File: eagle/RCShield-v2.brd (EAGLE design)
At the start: 92.7 x 82.5 mm, 52 parts, among them J1/J2 JOYSTICKPTH, P1/P3 POT, P2/P4 POT, Q1 MMBT3906, U1 TOUSCRUINO_SHIELD, U2 FT232RL-BASICSSOP, U4 XBEE, X1 USBSMD

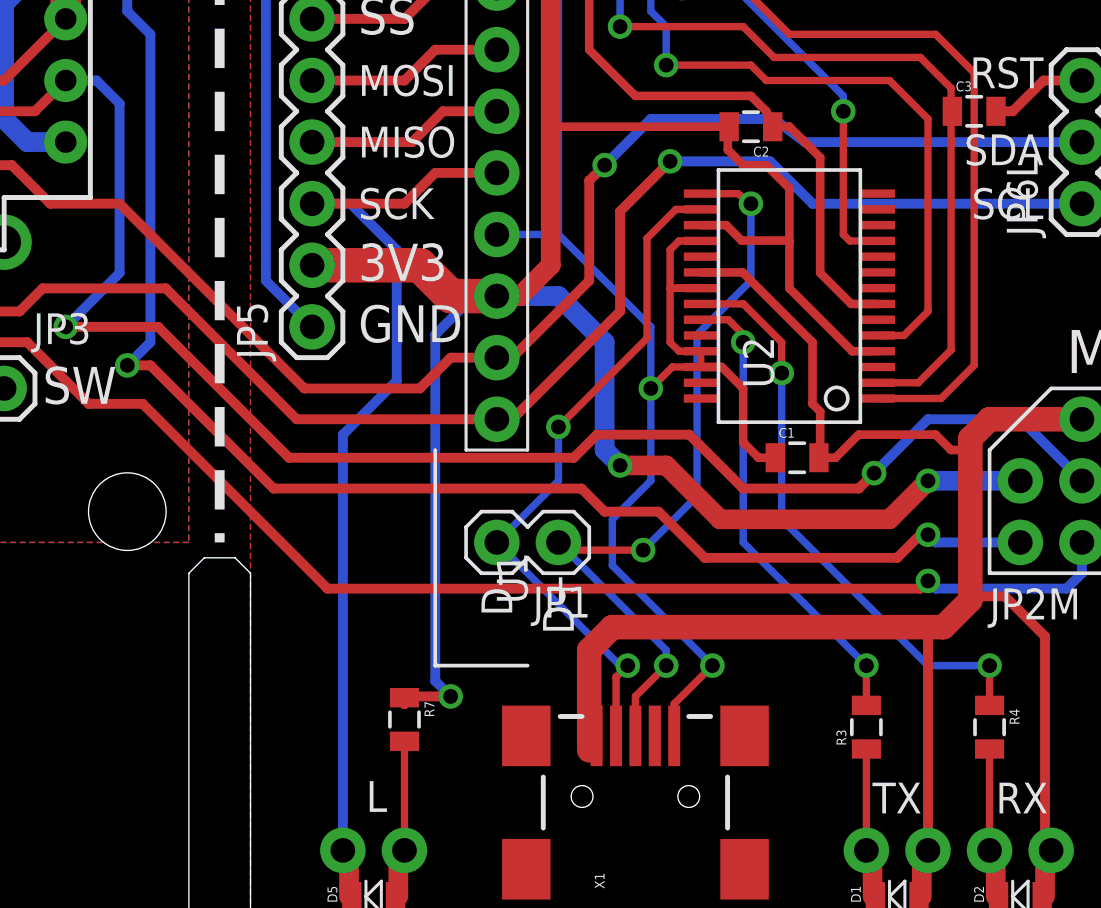
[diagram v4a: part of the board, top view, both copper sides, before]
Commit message: 
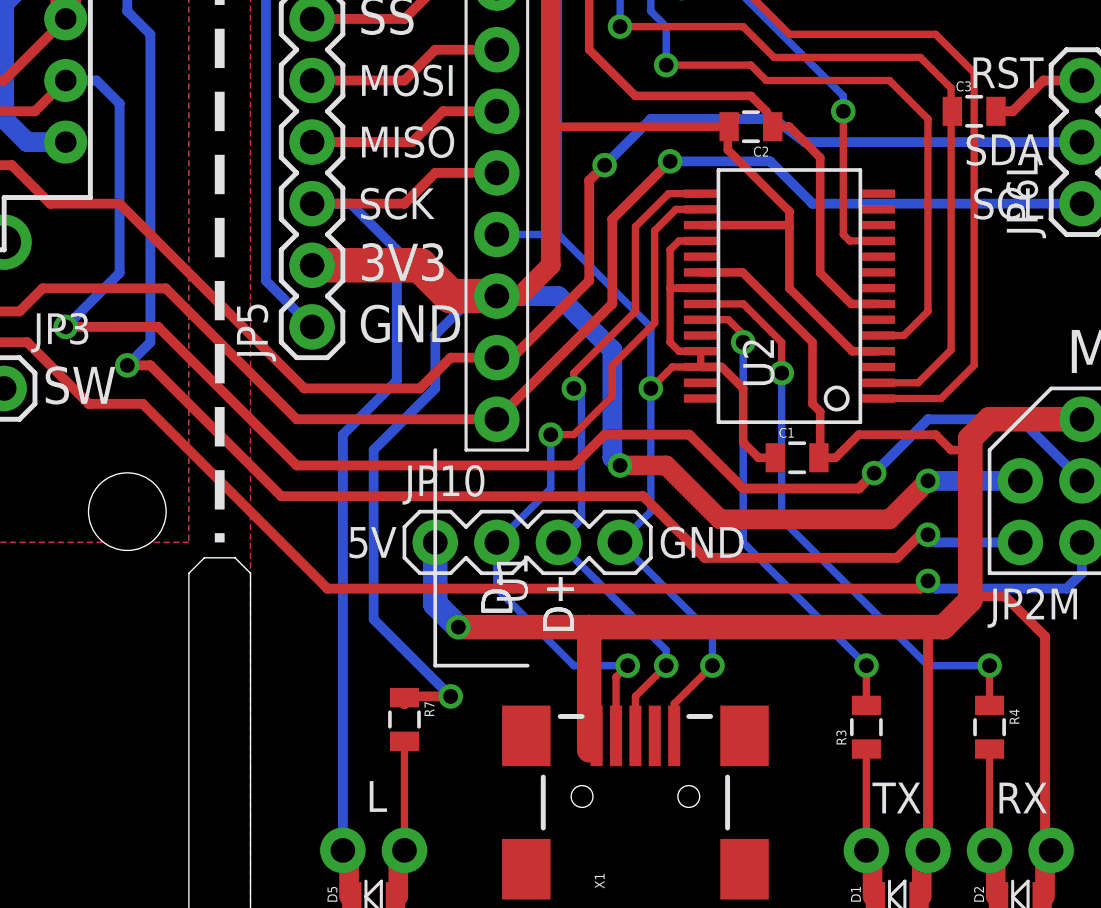
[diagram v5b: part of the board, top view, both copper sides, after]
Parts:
- removed JP1: USB, wibauxl:1X02
- added JP10: (no value), wibauxl:1X04
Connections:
- net D+: now also JP10.3; no longer JP1.1
- net D-: now also JP10.2; no longer JP1.2
- net GND: now also JP10.4
- net VUSB: now also JP10.1
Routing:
- net VUSB: track 74.1 -> 84.0 mm, vias 0 -> 1
- net D+: track 32.3 -> 28.2 mm, vias 3 -> 2
- net D-: track 28.4 -> 30.1 mm
- net 3.3V: track 348.7 -> 350.0 mm
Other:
- board text added: "5V"

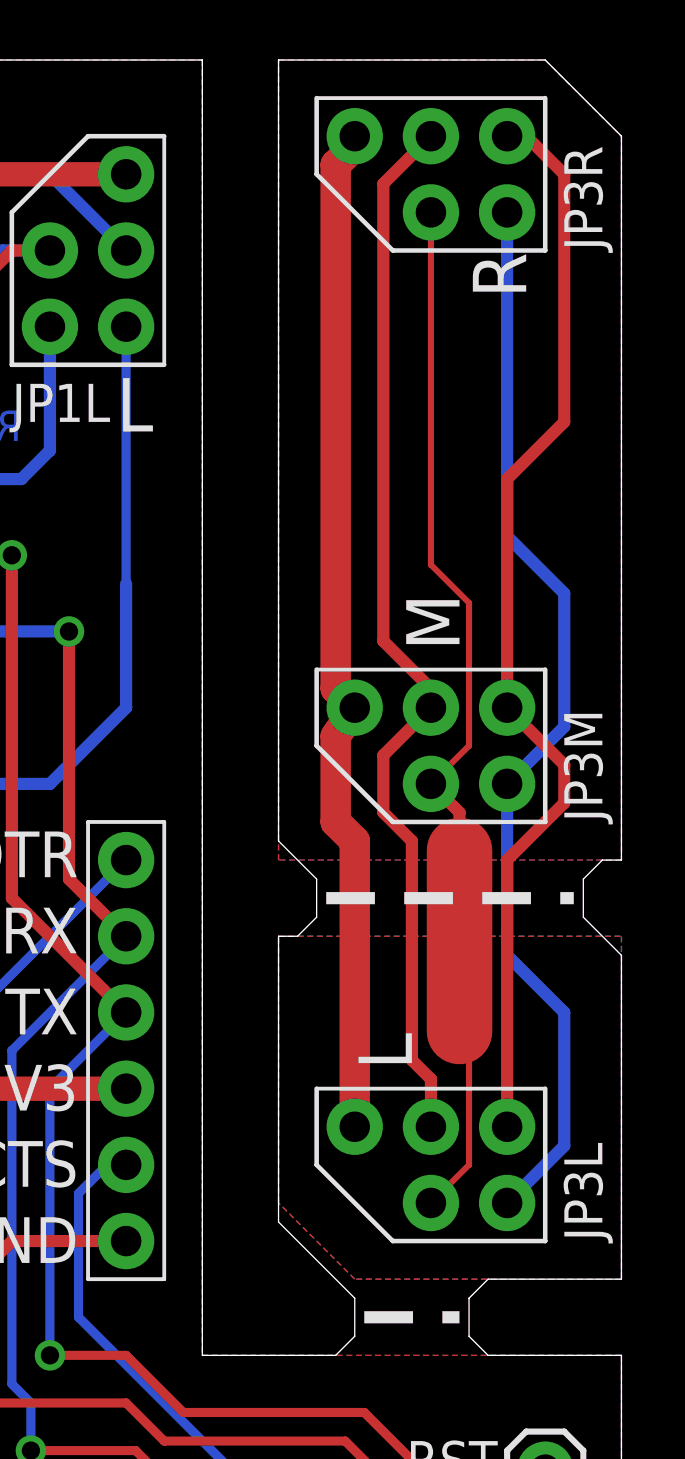
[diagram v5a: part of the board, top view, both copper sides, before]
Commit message: 
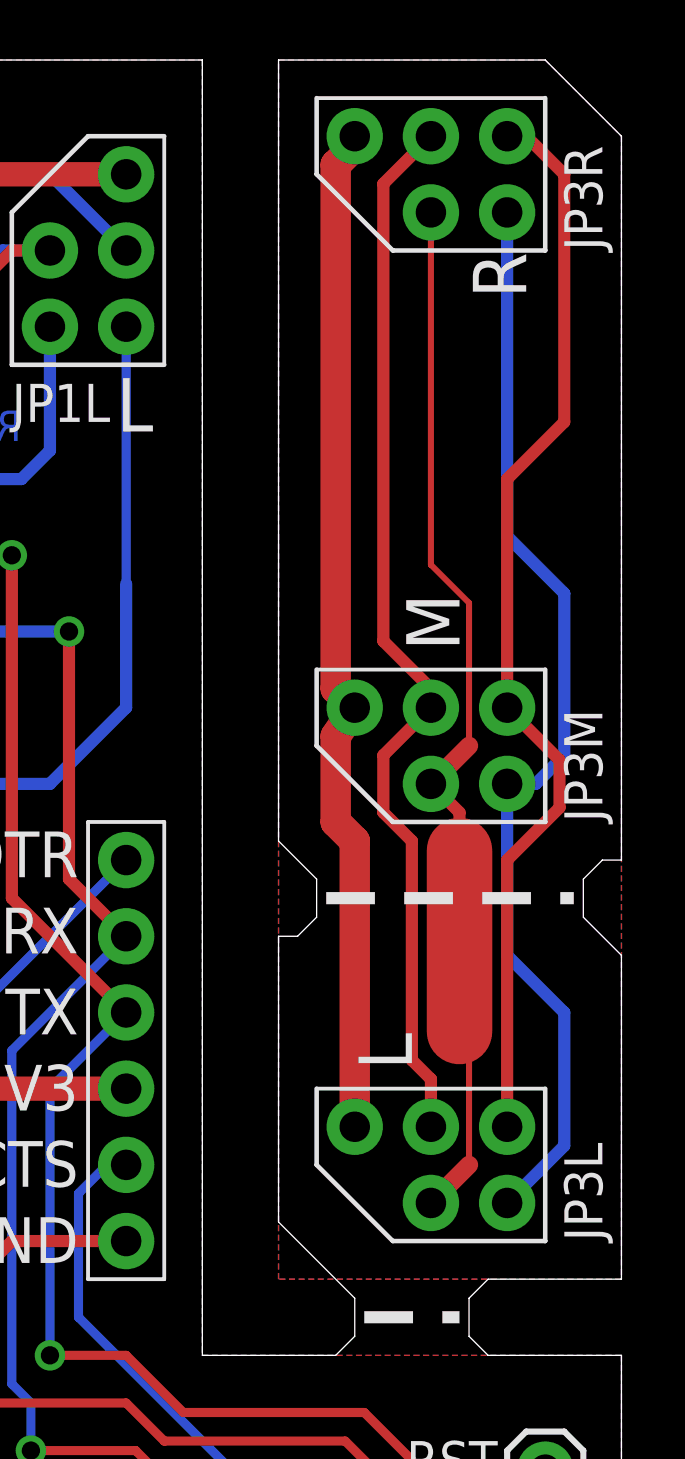
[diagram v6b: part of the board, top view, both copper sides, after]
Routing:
- net N$6: track 36.2 -> 36.7 mm
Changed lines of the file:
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@@
 <wire x1="90.805" y1="70.485" x2="88.9" y2="68.58" width="0.4064" layer="1"/>
 <wire x1="88.9" y1="68.58" x2="88.9" y2="60.96" width="0.4064" layer="1"/>
-<wire x1="88.9" y1="60.96" x2="90.805" y2="59.055" width="0.4064" layer="1"/>
-<wire x1="90.805" y1="59.055" x2="90.805" y2="57.785" width="0.4064" layer="1"/>
-<wire x1="90.805" y1="57.785" x2="88.9" y2="55.88" width="0.4064" layer="1"/>
+<wire x1="88.9" y1="60.96" x2="90.64625" y2="59.21375" width="0.4064" layer="1"/>
+<wire x1="90.64625" y1="59.21375" x2="90.64625" y2="57.62625" width="0.4064" layer="1"/>
+<wire x1="90.64625" y1="57.62625" x2="88.9" y2="55.88" width="0.4064" layer="1"/>
 <wire x1="88.9" y1="55.88" x2="88.9" y2="46.99" width="0.4064" layer="1"/>
 </signal>
@@
 <wire x1="88.9" y1="77.47" x2="88.9" y2="66.675" width="0.4064" layer="16"/>
 <wire x1="88.9" y1="66.675" x2="90.805" y2="64.77" width="0.4064" layer="16"/>
-<wire x1="90.805" y1="64.77" x2="90.805" y2="60.325" width="0.4064" layer="16"/>
-<wire x1="90.805" y1="60.325" x2="88.9" y2="58.42" width="0.4064" layer="16"/>
+<wire x1="90.805" y1="64.77" x2="90.805" y2="59.3725" width="0.4064" layer="16"/>
+<wire x1="90.805" y1="59.3725" x2="89.8525" y2="58.42" width="0.4064" layer="16"/>
+<wire x1="89.8525" y1="58.42" x2="88.9" y2="58.42" width="0.4064" layer="16"/>
 <wire x1="88.9" y1="58.42" x2="88.9" y2="52.705" width="0.4064" layer="16"/>
 <wire x1="88.9" y1="52.705" x2="90.805" y2="50.8" width="0.4064" layer="16"/>
@@
 <contactref element="JP3L" pad="1"/>
 <contactref element="JP3M" pad="1"/>
-<polygon width="0.254" layer="16" thermals="no">
+<polygon width="0.254" layer="16">
 <vertex x="81.28" y="82.55"/>
 <vertex x="90.17" y="82.55"/>
 <vertex x="92.71" y="80.01"/>
-<vertex x="92.71" y="55.88"/>
-<vertex x="81.28" y="55.88"/>
+<vertex x="92.71" y="41.91"/>
+<vertex x="81.28" y="41.91"/>
 </polygon>
-<polygon width="0.254" layer="1" thermals="no">
+<polygon width="0.254" layer="1">
 <vertex x="81.28" y="82.55"/>
 <vertex x="90.17" y="82.55"/>
 <vertex x="92.71" y="80.01"/>
-<vertex x="92.71" y="55.88"/>
-<vertex x="81.28" y="55.88"/>
-</polygon>
-<polygon width="0.254" layer="16">
-<vertex x="81.28" y="53.34"/>
-<vertex x="92.71" y="53.34"/>
 <vertex x="92.71" y="41.91"/>
-<vertex x="83.82" y="41.91"/>
-<vertex x="81.28" y="44.45"/>
-</polygon>
-<polygon width="0.254" layer="1">
-<vertex x="81.28" y="53.34"/>
-<vertex x="92.71" y="53.34"/>
-<vertex x="92.71" y="41.91"/>
-<vertex x="83.82" y="41.91"/>
-<vertex x="81.28" y="44.45"/>
+<vertex x="81.28" y="41.91"/>
 </polygon>
 <wire x1="86.36" y1="77.47" x2="86.36" y2="65.7225" width="0.2032" layer="1"/>
 <wire x1="86.36" y1="65.7225" x2="87.63" y2="64.4525" width="0.2032" layer="1"/>
 <wire x1="87.63" y1="64.4525" x2="87.63" y2="59.69" width="0.2032" layer="1"/>
-<wire x1="87.63" y1="59.69" x2="86.36" y2="58.42" width="0.2032" layer="1"/>
+<wire x1="87.63" y1="59.69" x2="86.36" y2="58.42" width="0.6096" layer="1"/>
 <wire x1="86.36" y1="58.42" x2="87.3125" y2="57.4675" width="0.4064" layer="1"/>
 <wire x1="87.3125" y1="57.4675" x2="87.3125" y2="56.1975" width="0.4064" layer="1"/>
@@
 <wire x1="87.3125" y1="50.165" x2="87.63" y2="49.8475" width="0.3048" layer="1"/>
 <wire x1="87.63" y1="49.8475" x2="87.63" y2="45.72" width="0.2032" layer="1"/>
-<wire x1="87.63" y1="45.72" x2="86.36" y2="44.45" width="0.2032" layer="1"/>
+<wire x1="87.63" y1="45.72" x2="86.36" y2="44.45" width="0.6096" layer="1"/>
 </signal>
 <signal name="N$8">
